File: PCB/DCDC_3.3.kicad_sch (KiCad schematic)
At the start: 21 parts, among them U10 HT75xx-1-SOT89, U11 LV2842XLVDDCR

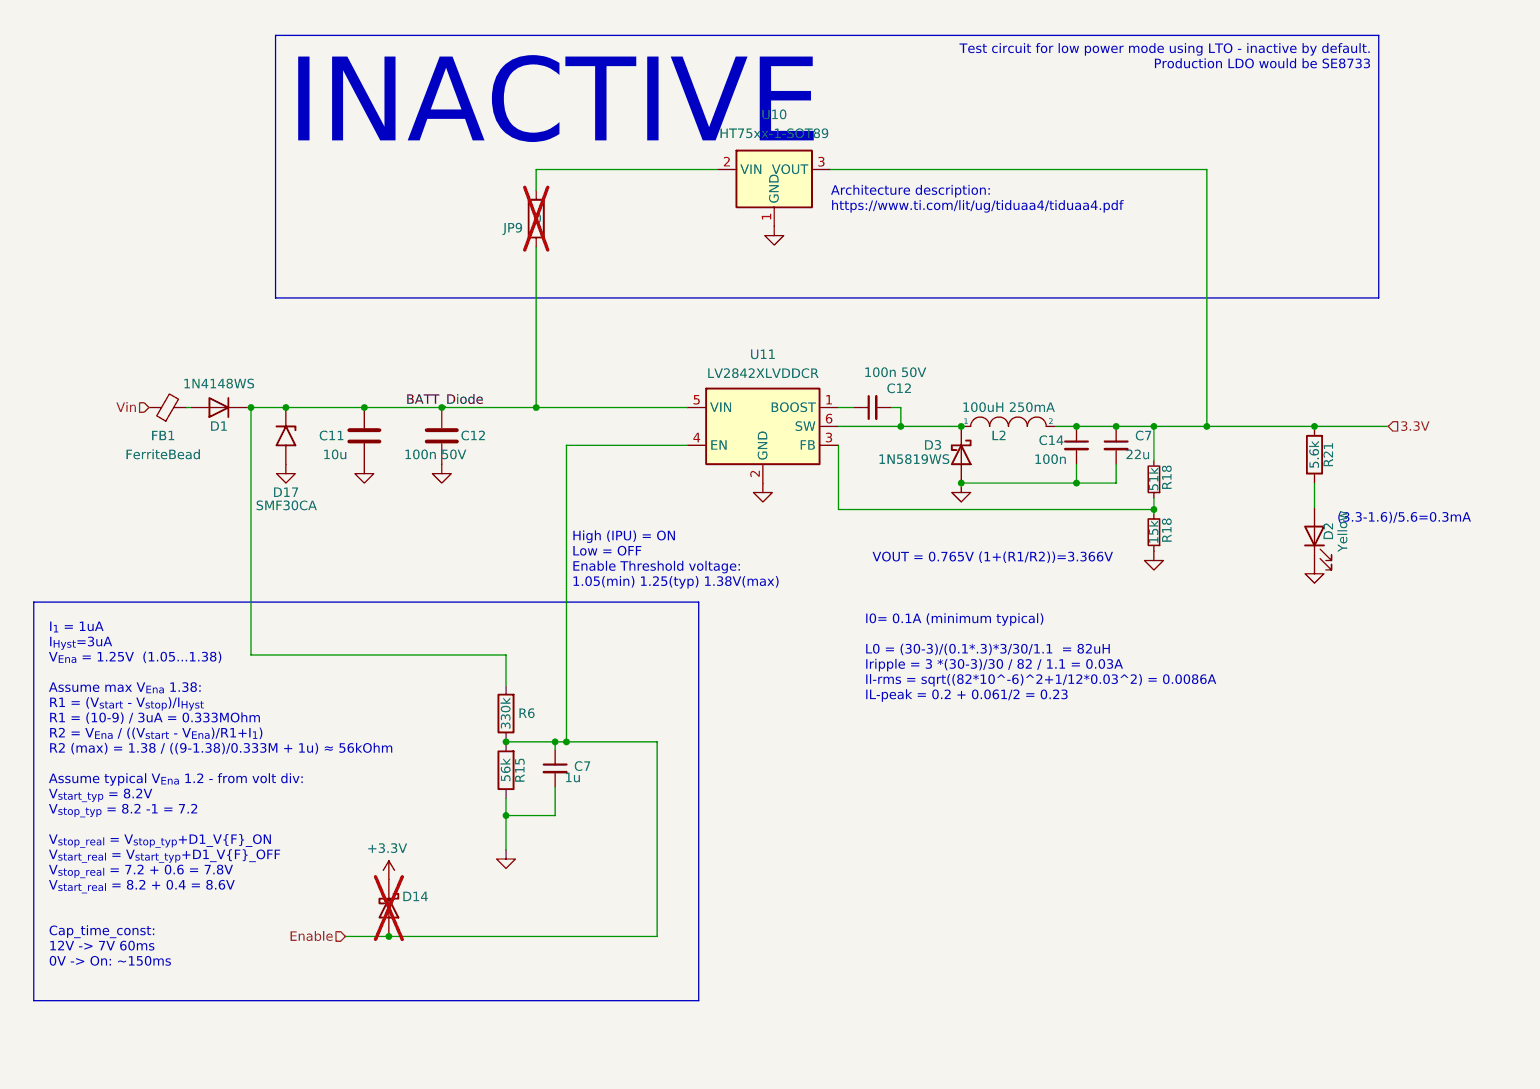
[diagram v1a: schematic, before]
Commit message: Removed test LDO regulator
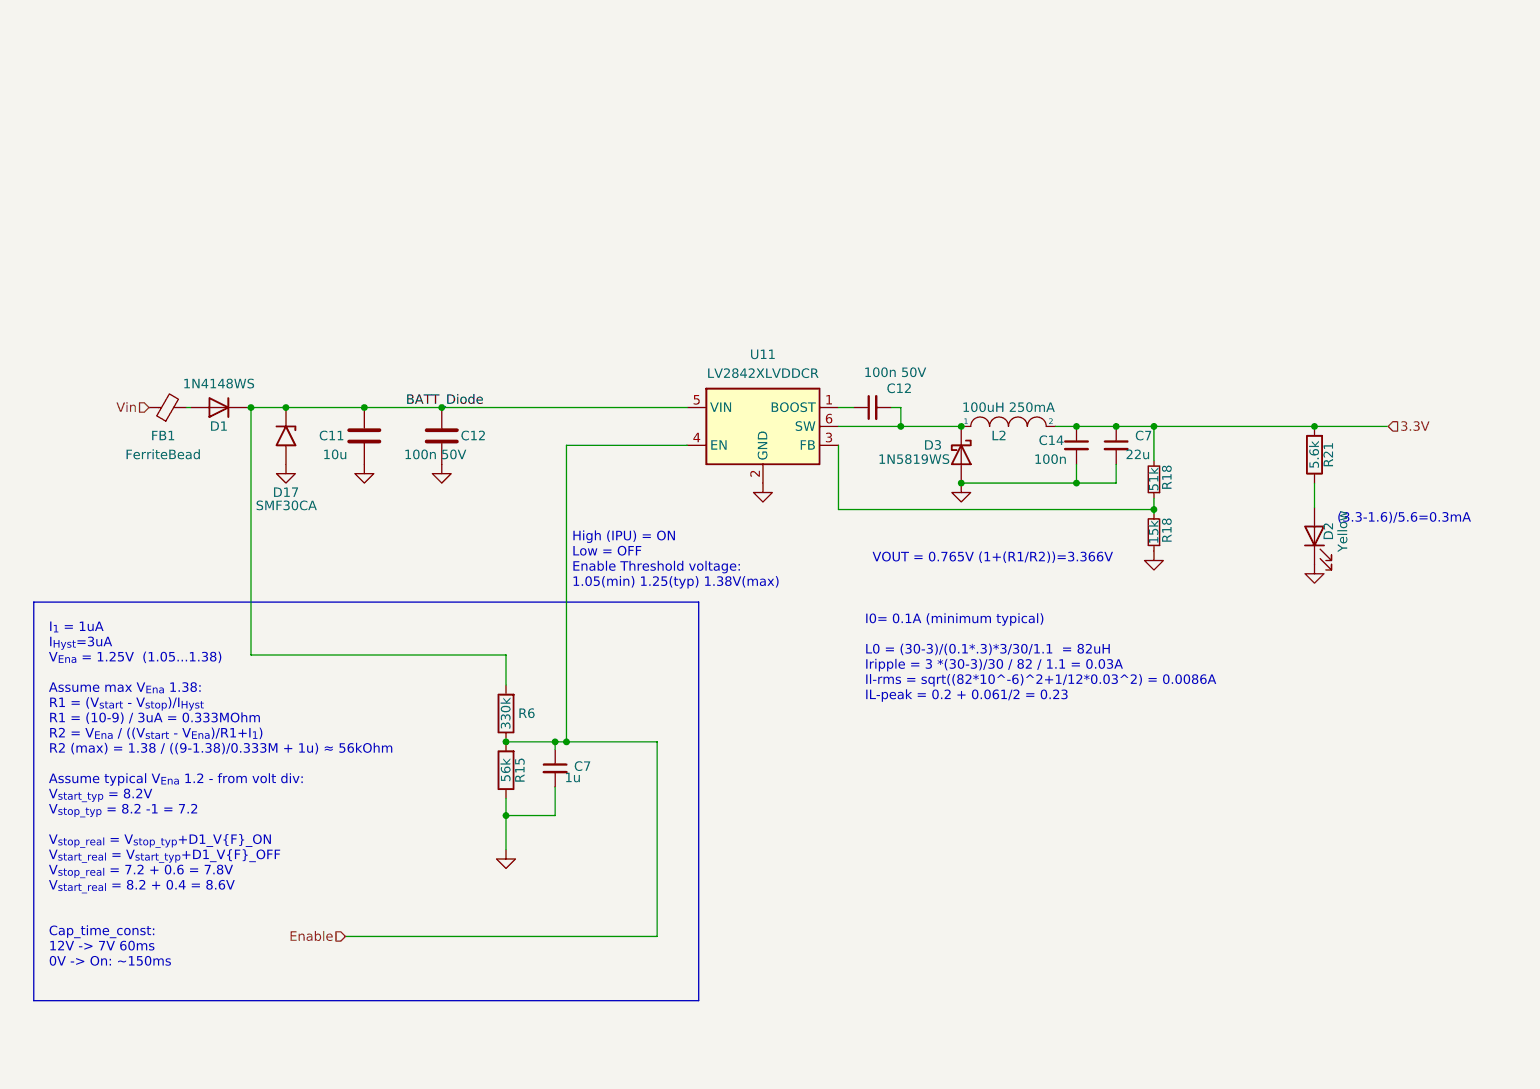
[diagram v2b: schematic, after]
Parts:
- removed D14: 1N5819WS, Diode_SMD:D_SOD-323, symbol Diode:1N5819
- removed JP9: 0, Resistor_SMD:R_0805_2012Metric, symbol Device:R
- removed U10: HT75xx-1-SOT89, Package_TO_SOT_SMD:SOT-89-3, symbol Regulator_Linear:HT75xx-1-SOT89
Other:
- note removed: "Architecture description: https://www.ti.com/lit/ug/tiduaa4/tiduaa4.pdf"
- note removed: "INACTIVE"
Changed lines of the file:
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@@
   (junction (at 101.6 134.874) (diameter 0) (color 0 0 0 0)
   )
-  (junction (at 105.664 80.01) (diameter 0) (color 0 0 0 0)
-  )
   (junction (at 210.312 82.55) (diameter 0) (color 0 0 0 0)
   )
@@
   (junction (at 162.814 82.55) (diameter 0) (color 0 0 0 0)
   )
-  (junction (at 195.834 82.55) (diameter 0) (color 0 0 0 0)
-  )
   (junction (at 92.964 80.01) (diameter 0) (color 0 0 0 0)
   )
@@
   (junction (at 188.722 82.55) (diameter 0) (color 0 0 0 0)
   )
-  (junction (at 85.852 151.13) (diameter 0) (color 0 0 0 0)
-  )
   (junction (at 101.6 124.968) (diameter 0) (color 0 0 0 0)
   )
@@
     (stroke (width 0) (type default))
   )
-  (wire (pts (xy 105.664 48.006) (xy 105.664 50.8))
-    (stroke (width 0) (type default))
-  )
   (wire (pts (xy 146.304 85.09) (xy 146.304 93.726))
     (stroke (width 0) (type default))
@@
     (stroke (width 0) (type default))
   )
-  (wire (pts (xy 195.834 82.55) (xy 210.312 82.55))
+  (wire (pts (xy 188.722 82.55) (xy 210.312 82.55))
     (stroke (width 0) (type default))
   )
@@
     (stroke (width 0) (type default))
   )
-  (wire (pts (xy 188.722 82.55) (xy 195.834 82.55))
-    (stroke (width 0) (type default))
-  )
   (wire (pts (xy 178.308 90.17) (xy 183.642 90.17))
     (stroke (width 0) (type default))
   )
-  (wire (pts (xy 92.964 80.01) (xy 105.664 80.01))
-    (stroke (width 0) (type default))
-  )
   (wire (pts (xy 154.686 82.55) (xy 162.814 82.55))
     (stroke (width 0) (type default))
@@
     (stroke (width 0) (type default))
   )
-  (wire (pts (xy 80.01 151.13) (xy 85.852 151.13))
-    (stroke (width 0) (type default))
-  )
-  (wire (pts (xy 145.288 48.006) (xy 195.834 48.006))
+  (wire (pts (xy 80.01 151.13) (xy 121.92 151.13))
     (stroke (width 0) (type default))
   )
@@
     (stroke (width 0) (type default))
   )
-  (wire (pts (xy 195.834 48.006) (xy 195.834 82.55))
-    (stroke (width 0) (type default))
-  )
   (wire (pts (xy 210.312 90.17) (xy 210.312 93.472))
     (stroke (width 0) (type default))
@@
     (stroke (width 0) (type default))
   )
-  (wire (pts (xy 105.664 48.006) (xy 130.048 48.006))
-    (stroke (width 0) (type default))
-  )
   (wire (pts (xy 108.204 134.874) (xy 101.6 134.874))
     (stroke (width 0) (type default))
@@
     (stroke (width 0) (type default))
   )
-  (wire (pts (xy 105.664 80.01) (xy 125.984 80.01))
+  (wire (pts (xy 92.964 80.01) (xy 125.984 80.01))
     (stroke (width 0) (type default))
   )
@@
     (stroke (width 0) (type default))
   )
-  (wire (pts (xy 85.852 151.13) (xy 121.92 151.13))
-    (stroke (width 0) (type default))
-  )
   (wire (pts (xy 101.6 124.968) (xy 108.204 124.968))
     (stroke (width 0) (type default))
@@
     (stroke (width 0) (type default))
   )
-  (wire (pts (xy 105.664 58.42) (xy 105.664 80.01))
-    (stroke (width 0) (type default))
-  )
   (rectangle (start 38.1 106.172) (end 127.508 159.766)
     (stroke (width 0) (type default))
     (fill (type none))
-  )
-  (text_box "Test circuit for low power mode using LTO - inactive by default.\nProduction LDO would be SE8733"
-    (at 70.612 29.972 0) (size 148.336 35.306)
-    (stroke (width 0) (type default))
-    (fill (type none))
-    (effects (font (size 1.27 1.27)) (justify right top))
   )
   (text "(3.3-1.6)/5.6=0.3mA" (at 213.36 95.758 0)
@@
     (effects (font (size 1.27 1.27)) (justify left bottom))
   )
-  (text "INACTIVE" (at 72.136 45.72 0)
-    (effects (font (size 11.27 11.27)) (justify left bottom))
-  )
   (text "VOUT = 0.765V (1+(R1/R2))=3.366V" (at 150.876 101.092 0)
     (effects (font (size 1.27 1.27)) (justify left bottom))
   )
-  (text "Architecture description:\nhttps://www.ti.com/lit/ug/tiduaa4/tiduaa4.pdf"
-    (at 145.288 53.848 0)
-    (effects (font (size 1.27 1.27)) (justify left bottom) (href "https://www.ti.com/lit/ug/tiduaa4/tiduaa4.pdf"))
-  )
   (label "BATT_Diode" (at 88.138 80.01 0) (fields_autoplaced)
     (effects (font (size 1.27 1.27)) (justify left bottom))
@@
         (path "/92dad13e-412a-43d4-9260-9087579302b1/82f027ad-2d00-453d-ab1c-0ba3b5cb1ef7"
           (reference "D21") (unit 1)
-        )
-      )
-    )
-  )
-  (symbol (lib_id "Diode:1N5819") (at 85.852 147.32 270) (unit 1)
-    (in_bom yes) (on_board yes) (dnp yes)
-    (property "Reference" "D14" (at 89.408 145.796 90)
-      (effects (font (size 1.27 1.27)))
-    )
-    (property "Value" "1N5819WS" (at 92.456 147.828 90)
-      (effects (font (size 1.27 1.27)) hide)
-    )
-    (property "Footprint" "Diode_SMD:D_SOD-323" (at 81.407 147.32 0)
-      (effects (font (size 1.27 1.27)) hide)
-    )
-    (property "Datasheet" "https://datasheet.lcsc.com/lcsc/2204281430_Guangdong-Hottech-1N5819WS_C191023.pdf" (at 85.852 147.32 0)
-      (effects (font (size 1.27 1.27)) hide)
-    )
-    (property "LCSC" "C191023" (at 78.867 147.0025 0)
-      (effects (font (size 1.27 1.27)) hide)
-    )
-    (pin "1")
-    (pin "2")
-    (instances
-      (project "StepperServoCAN"
-        (path "/92dad13e-412a-43d4-9260-9087579302b1"
-          (reference "D14") (unit 1)
-        )
-        (path "/92dad13e-412a-43d4-9260-9087579302b1/82f027ad-2d00-453d-ab1c-0ba3b5cb1ef7"
-          (reference "D22") (unit 1)
         )
       )
@@
     )
   )
-  (symbol (lib_id "Regulator_Linear:HT75xx-1-SOT89") (at 137.668 50.546 0) (unit 1)
-    (in_bom yes) (on_board yes) (dnp no) (fields_autoplaced)
-    (property "Reference" "U10" (at 137.668 40.64 0)
-      (effects (font (size 1.27 1.27)))
-    )
-    (property "Value" "HT75xx-1-SOT89" (at 137.668 43.18 0)
-      (effects (font (size 1.27 1.27)))
-    )
-    (property "Footprint" "Package_TO_SOT_SMD:SOT-89-3" (at 137.668 42.291 0)
-      (effects (font (size 1.27 1.27) italic) hide)
-    )
-    (property "Datasheet" "https://datasheet.lcsc.com/lcsc/1811062113_Holtek-Semicon-HT7533-1_C14289.pdf" (at 137.668 48.006 0)
-      (effects (font (size 1.27 1.27)) hide)
-    )
-    (property "LSCS" "" (at 137.668 50.546 0)
-      (effects (font (size 1.27 1.27)) hide)
-    )
-    (property "LCSC" "C14289" (at 137.668 50.546 0)
-      (effects (font (size 1.27 1.27)) hide)
-    )
-    (pin "1")
-    (pin "2")
-    (pin "3")
-    (instances
-      (project "StepperServoCAN"
-        (path "/92dad13e-412a-43d4-9260-9087579302b1/82f027ad-2d00-453d-ab1c-0ba3b5cb1ef7"
-          (reference "U10") (unit 1)
-        )
-      )
-    )
-  )
-  (symbol (lib_id "power:+3.3V") (at 85.852 143.51 0) (unit 1)
-    (in_bom yes) (on_board yes) (dnp no)
-    (property "Reference" "#PWR06" (at 85.852 147.32 0)
-      (effects (font (size 1.27 1.27)) hide)
-    )
-    (property "Value" "+3.3V" (at 85.6039 139.3021 0)
-      (effects (font (size 1.27 1.27)))
-    )
-    (property "Footprint" "" (at 85.852 143.51 0)
-      (effects (font (size 1.27 1.27)) hide)
-    )
-    (property "Datasheet" "" (at 85.852 143.51 0)
-      (effects (font (size 1.27 1.27)) hide)
-    )
-    (pin "1")
-    (instances
-      (project "StepperServoCAN"
-        (path "/92dad13e-412a-43d4-9260-9087579302b1"
-          (reference "#PWR06") (unit 1)
-        )
-        (path "/92dad13e-412a-43d4-9260-9087579302b1/82f027ad-2d00-453d-ab1c-0ba3b5cb1ef7"
-          (reference "#PWR099") (unit 1)
-        )
-      )
-    )
-  )
-  (symbol (lib_id "power:GND") (at 137.668 55.626 0) (unit 1)
-    (in_bom yes) (on_board yes) (dnp no)
-    (property "Reference" "#PWR019" (at 137.668 61.976 0)
-      (effects (font (size 1.27 1.27)) hide)
-    )
-    (property "Value" "GND" (at 138.938 58.166 0)
-      (effects (font (size 1.27 1.27)) (justify left) hide)
-    )
-    (property "Footprint" "" (at 137.668 55.626 0)
-      (effects (font (size 1.27 1.27)) hide)
-    )
-    (property "Datasheet" "" (at 137.668 55.626 0)
-      (effects (font (size 1.27 1.27)) hide)
-    )
-    (pin "1")
-    (instances
-      (project "StepperServoCAN"
-        (path "/92dad13e-412a-43d4-9260-9087579302b1"
-          (reference "#PWR019") (unit 1)
-        )
-        (path "/92dad13e-412a-43d4-9260-9087579302b1/82f027ad-2d00-453d-ab1c-0ba3b5cb1ef7"
-          (reference "#PWR090") (unit 1)
-        )
-      )
-    )
-  )
   (symbol (lib_id "Device:R_Small") (at 188.722 89.662 180) (unit 1)
     (in_bom yes) (on_board yes) (dnp no)
@@
         )
       )
-    )
-  )
-  (symbol (lib_id "Device:R") (at 105.664 54.61 180) (unit 1)
-    (in_bom no) (on_board yes) (dnp yes)
-    (property "Reference" "JP9" (at 103.886 55.88 0)
-      (effects (font (size 1.27 1.27)) (justify left))
-    )
-    (property "Value" "0" (at 106.426 54.61 0)
-      (effects (font (size 1.27 1.27)) (justify left))
-    )
-    (property "Footprint" "Resistor_SMD:R_0805_2012Metric" (at 107.442 54.61 90)
-      (effects (font (size 1.27 1.27)) hide)
-    )
-    (property "Datasheet" "~" (at 105.664 54.61 0)
-      (effects (font (size 1.27 1.27)) hide)
-    )
-    (property "LSCS" "" (at 105.664 54.61 0)
-      (effects (font (size 1.27 1.27)) hide)
-    )
-    (property "LCSC" "C21189" (at 105.664 54.61 0)
-      (effects (font (size 1.27 1.27)) hide)
-    )
-    (pin "1")
-    (pin "2")
-    (instances
-      (project "StepperServoCAN"
-        (path "/92dad13e-412a-43d4-9260-9087579302b1/82f027ad-2d00-453d-ab1c-0ba3b5cb1ef7"
-          (reference "JP9") (unit 1)
-        )
-      )

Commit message: Kicad8. Also clear zone filling before saving
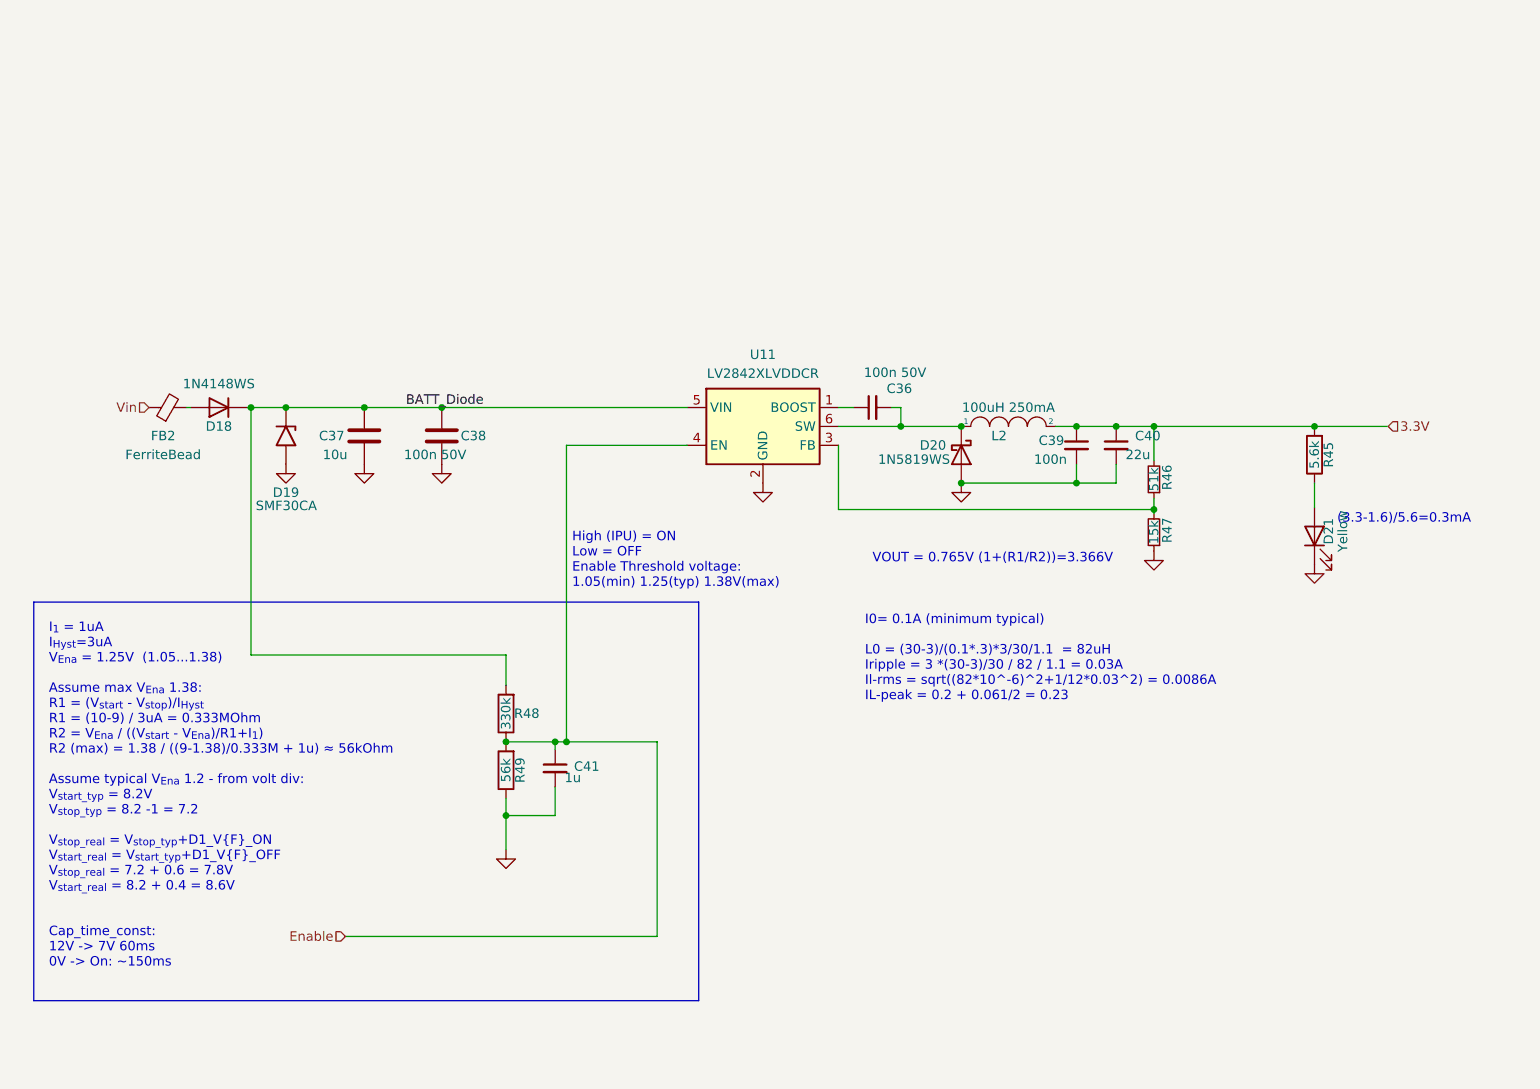
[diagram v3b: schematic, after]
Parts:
- renumbered C12 to C36, C11 to C37, C12 to C38, C14 to C39, C7 to C40, C7 to C41, D1 to D18, D17 to D19, D3 to D20, D2 to D21, FB1 to FB2, R21 to R45, R18 to R46, R18 to R47, R6 to R48, R15 to R49
